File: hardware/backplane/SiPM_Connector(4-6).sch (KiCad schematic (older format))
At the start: 8 parts, among them J401 Conn_02x34_Odd_Even, J402 ERF8-060-05.0-L-DV, J403 Conn_02x34_Odd_Even, J501 Conn_02x34_Odd_Even-Connector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, J503 Conn_02x34_Odd_Even-Connector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, J601 Conn_02x34_Odd_Even-Connector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, J602 ERF8-060-05.0-L-DV, J603 Conn_02x34_Odd_Even-Connector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

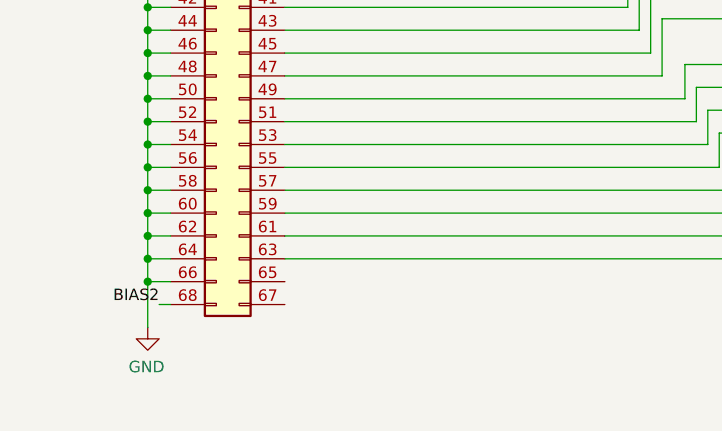
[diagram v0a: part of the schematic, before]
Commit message: Readout_FMC started
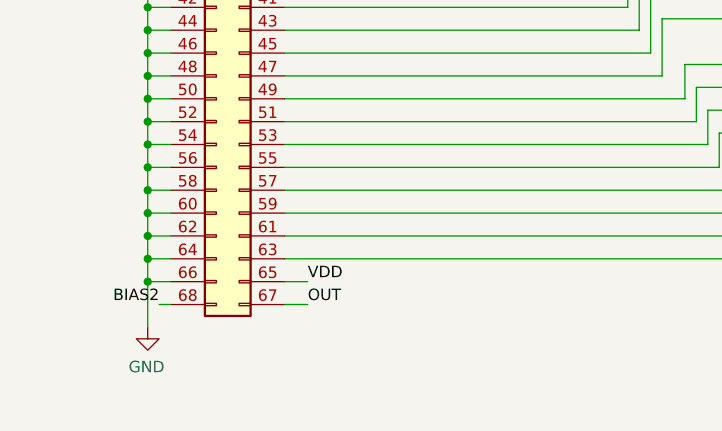
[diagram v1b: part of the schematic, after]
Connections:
- net OUT: now also J601.67 (Pin_67)
- net VDD: now also J601.65 (Pin_65)
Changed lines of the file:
@@
 	2050 4150 2050 4350
 $Comp
-L backplane-prototype-rescue:GND-power #PWR01
+L backplane-prototype-rescue:GND-power #PWR0107
 U 1 1 60B6FC2F
 P 2050 4350
-F 0 "#PWR01" H 2050 4100 50  0001 C CNN
+F 0 "#PWR0107" H 2050 4100 50  0001 C CNN
 F 1 "GND" H 2055 4177 50  0000 C CNN
 F 2 "" H 2050 4350 50  0001 C CNN
@@
 	8950 4150 8950 4350
 $Comp
-L backplane-prototype-rescue:GND-power #PWR06
+L backplane-prototype-rescue:GND-power #PWR0108
 U 1 1 60B6FC31
 P 8950 4350
-F 0 "#PWR06" H 8950 4100 50  0001 C CNN
+F 0 "#PWR0108" H 8950 4100 50  0001 C CNN
 F 1 "GND" H 8955 4177 50  0000 C CNN
 F 2 "" H 8950 4350 50  0001 C CNN
@@
 Connection ~ 6100 4600
 $Comp
-L backplane-prototype-rescue:GND-power #PWR0101
+L backplane-prototype-rescue:GND-power #PWR0109
 U 1 1 60B6FC33
 P 4900 13500
-F 0 "#PWR0101" H 4900 13250 50  0001 C CNN
+F 0 "#PWR0109" H 4900 13250 50  0001 C CNN
 F 1 "GND" H 4905 13327 50  0000 C CNN
 F 2 "" H 4900 13500 50  0001 C CNN
@@
 $EndComp
 $Comp
-L backplane-prototype-rescue:GND-power #PWR0102
+L backplane-prototype-rescue:GND-power #PWR0110
 U 1 1 63C65F05
 P 6100 13500
-F 0 "#PWR0102" H 6100 13250 50  0001 C CNN
+F 0 "#PWR0110" H 6100 13250 50  0001 C CNN
 F 1 "GND" H 6105 13327 50  0000 C CNN
 F 2 "" H 6100 13500 50  0001 C CNN
@@
 	2050 8700 2050 8900
 $Comp
-L backplane-prototype-rescue:GND-power #PWR?
+L backplane-prototype-rescue:GND-power #PWR0111
 U 1 1 63C65F08
 P 2050 8900
-F 0 "#PWR?" H 2050 8650 50  0001 C CNN
+F 0 "#PWR0111" H 2050 8650 50  0001 C CNN
 F 1 "GND" H 2055 8727 50  0000 C CNN
 F 2 "" H 2050 8900 50  0001 C CNN
@@
 	2050 13150 2050 13350
 $Comp
-L backplane-prototype-rescue:GND-power #PWR?
+L backplane-prototype-rescue:GND-power #PWR0112
 U 1 1 63C65F09
 P 2050 13350
-F 0 "#PWR?" H 2050 13100 50  0001 C CNN
+F 0 "#PWR0112" H 2050 13100 50  0001 C CNN
 F 1 "GND" H 2055 13177 50  0000 C CNN
 F 2 "" H 2050 13350 50  0001 C CNN
@@
 	8950 8700 8950 8900
 $Comp
-L backplane-prototype-rescue:GND-power #PWR?
+L backplane-prototype-rescue:GND-power #PWR0113
 U 1 1 63C65F0A
 P 8950 8900
-F 0 "#PWR?" H 8950 8650 50  0001 C CNN
+F 0 "#PWR0113" H 8950 8650 50  0001 C CNN
 F 1 "GND" H 8955 8727 50  0000 C CNN
 F 2 "" H 8950 8900 50  0001 C CNN
@@
 	8950 13150 8950 13350
 $Comp
-L backplane-prototype-rescue:GND-power #PWR?
+L backplane-prototype-rescue:GND-power #PWR0114
 U 1 1 63C65F0B
 P 8950 13350
-F 0 "#PWR?" H 8950 13100 50  0001 C CNN
+F 0 "#PWR0114" H 8950 13100 50  0001 C CNN
 F 1 "GND" H 8955 13177 50  0000 C CNN
 F 2 "" H 8950 13350 50  0001 C CNN
@@
 Wire Wire Line
 	8900 8800 8900 8900
+Text Label 2750 13150 0    50   ~ 0
+VDD
+Text Label 2750 13250 0    50   ~ 0
+OUT
+Wire Wire Line
+	2750 13250 2650 13250
+Wire Wire Line
+	2750 13150 2650 13150
 $EndSCHEMATC

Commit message: Backplane Layout Started
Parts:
- removed J401, J403: Conn_02x34_Odd_Even, Backplane-prototype:SAMTEC_CLM-134-02-F-D, symbol backplane-prototype-rescue:Conn_02x34_Odd_Even-Connector_Generic
- removed J402, J602: ERF8-060-05.0-L-DV, Backplane-prototype:ERF8-060-05.0-L-DV, symbol backplane-prototype-rescue:ERF8-060-XX.X-X-DV-ERF8-060-05.0-L-DV
- removed J501, J503, J601, J603: Conn_02x34_Odd_Even-Connector_Generic, symbol backplane-prototype-rescue:Conn_02x34_Odd_Even-Connector_Generic
- added J101, J103: Conn_02x34_Odd_Even, backplane:SAMTEC_CLM-134-02-F-D, symbol backplane-rescue:Conn_02x34_Odd_Even-Connector_Generic-backplane-prototype-resc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
- added J201, J203, J301, J303: Conn_02x34_Odd_Even-Connector_Generic, backplane:SAMTEC_CLM-134-02-F-D, symbol backplane-rescue:Conn_02x34_Odd_Even-Connector_Generic-backplane-prototype-resc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
- added J402, J602: ERF8-060-05.0-L-DV, backplane:ERF8-060-05.0-L-DV, symbol backplane-rescue:ERF8-060-XX.X-X-DV-ERF8-060-05.0-L-DV-backplane-prototype-resc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
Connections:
- net BCH0: now also J103.67 (Pin_67), J402.3
- net BCH1: now also J103.65 (Pin_65), J402.5
- net BCH10: now also J103.47 (Pin_47), J402.25
- net BCH11: now also J103.45 (Pin_45), J402.27
- net BCH12: now also J103.43 (Pin_43), J402.29
- net BCH13: now also J103.41 (Pin_41), J402.31
- net BCH14: now also J103.39 (Pin_39), J402.33
- net BCH15: now also J103.37 (Pin_37), J402.35
- net BCH16: now also J103.35 (Pin_35), J402.39
- net BCH17: now also J103.33 (Pin_33), J402.41
- net BCH18: now also J103.31 (Pin_31), J402.43
- net BCH19: now also J103.29 (Pin_29), J402.45
- net BCH2: now also J103.63 (Pin_63), J402.7
- net BCH20: now also J103.27 (Pin_27), J402.47
- net BCH21: now also J103.25 (Pin_25), J402.49
- net BCH22: now also J103.23 (Pin_23), J402.51
- net BCH23: now also J103.21 (Pin_21), J402.53
- net BCH24: now also J103.19 (Pin_19), J402.57
- net BCH25: now also J103.17 (Pin_17), J402.59
- net BCH26: now also J103.15 (Pin_15), J402.61
- net BCH27: now also J103.13 (Pin_13), J402.63
- net BCH28: now also J103.11 (Pin_11), J402.65
- net BCH29: now also J103.9 (Pin_9), J402.67
- net BCH3: now also J103.61 (Pin_61), J402.9
- net BCH30: now also J103.7 (Pin_7), J402.69
- net BCH31: now also J103.5 (Pin_5), J402.71
- net BCH4: now also J103.59 (Pin_59), J402.11
- net BCH5: now also J103.57 (Pin_57), J402.13
- net BCH6: now also J103.55 (Pin_55), J402.15
- net BCH7: now also J103.53 (Pin_53), J402.17
- net BCH8: now also J103.51 (Pin_51), J402.21
- net BCH9: now also J103.49 (Pin_49), J402.23
- net BIAS1: now also J101.2 (Pin_2), J201.2 (Pin_2), J301.2 (Pin_2), J402.76, J602.116, J602.36
- net BIAS2: now also J101.68 (Pin_68), J201.68 (Pin_68), J301.68 (Pin_68), J402.80, J602.120, J602.40
- net BIAS3: now also J103.68 (Pin_68), J203.68 (Pin_68), J303.68 (Pin_68), J402.75, J602.115, J602.35
- net BIAS4: now also J103.2 (Pin_2), J203.2 (Pin_2), J303.2 (Pin_2), J402.79, J602.119, J602.39
- net CH0: now also J101.1 (Pin_1), J402.4
- net CH1: now also J101.3 (Pin_3), J402.6
- net CH10: now also J101.21 (Pin_21), J402.26
- net CH11: now also J101.23 (Pin_23), J402.28
- net CH12: now also J101.25 (Pin_25), J402.30
- net CH13: now also J101.27 (Pin_27), J402.32
- net CH14: now also J101.29 (Pin_29), J402.34
- net CH15: now also J101.31 (Pin_31), J402.36
- net CH16: now also J101.33 (Pin_33), J402.40
- net CH17: now also J101.35 (Pin_35), J402.42
- net CH18: now also J101.37 (Pin_37), J402.44
- net CH19: now also J101.39 (Pin_39), J402.46
- net CH2: now also J101.5 (Pin_5), J402.8
- net CH20: now also J101.41 (Pin_41), J402.48
- net CH21: now also J101.43 (Pin_43), J402.50
- net CH22: now also J101.45 (Pin_45), J402.52
- net CH23: now also J101.47 (Pin_47), J402.54
- net CH24: now also J101.49 (Pin_49), J402.58
- net CH25: now also J101.51 (Pin_51), J402.60
- net CH26: now also J101.53 (Pin_53), J402.62
- net CH27: now also J101.55 (Pin_55), J402.64
- net CH28: now also J101.57 (Pin_57), J402.66
- net CH29: now also J101.59 (Pin_59), J402.68
- net CH3: now also J101.7 (Pin_7), J402.10
- net CH30: now also J101.61 (Pin_61), J402.70
- net CH31: now also J101.63 (Pin_63), J402.72
- net CH4: now also J101.9 (Pin_9), J402.12
- net CH5: now also J101.11 (Pin_11), J402.14
- net CH6: now also J101.13 (Pin_13), J402.16
- net CH7: now also J101.15 (Pin_15), J402.18
- net CH8: now also J101.17 (Pin_17), J402.22
- net CH9: now also J101.19 (Pin_19), J402.24
- net GND: now also J101.10 (Pin_10), J101.12 (Pin_12), J101.14 (Pin_14), J101.16 (Pin_16), J101.18 (Pin_18), J101.20 (Pin_20), J101.22 (Pin_22), J101.24 (Pin_24), J101.26 (Pin_26), J101.28 (Pin_28), J101.30 (Pin_30), J101.32 (Pin_32), J101.34 (Pin_34), J101.36 (Pin_36), J101.38 (Pin_38), J101.4 (Pin_4), J101.40 (Pin_40), J101.42 (Pin_42), J101.44 (Pin_44), J101.46 (Pin_46), J101.48 (Pin_48), J101.50 (Pin_50), J101.52 (Pin_52), J101.54 (Pin_54), J101.56 (Pin_56), J101.58 (Pin_58), J101.6 (Pin_6), J101.60 (Pin_60), J101.62 (Pin_62), J101.64 (Pin_64), J101.66 (Pin_66), J101.8 (Pin_8), J103.10 (Pin_10), J103.12 (Pin_12), J103.14 (Pin_14), J103.16 (Pin_16), J103.18 (Pin_18), J103.20 (Pin_20), J103.22 (Pin_22), J103.24 (Pin_24), J103.26 (Pin_26), J103.28 (Pin_28), J103.30 (Pin_30), J103.32 (Pin_32), J103.34 (Pin_34), J103.36 (Pin_36), J103.38 (Pin_38), J103.4 (Pin_4), J103.40 (Pin_40), J103.42 (Pin_42), J103.44 (Pin_44), J103.46 (Pin_46), J103.48 (Pin_48), J103.50 (Pin_50), J103.52 (Pin_52), J103.54 (Pin_54), J103.56 (Pin_56), J103.58 (Pin_58), J103.6 (Pin_6), J103.60 (Pin_60), J103.62 (Pin_62), J103.64 (Pin_64), J103.66 (Pin_66), J103.8 (Pin_8), J201.10 (Pin_10), J201.12 (Pin_12), J201.14 (Pin_14), J201.16 (Pin_16), J201.18 (Pin_18), J201.20 (Pin_20), J201.22 (Pin_22), J201.24 (Pin_24), J201.26 (Pin_26), J201.28 (Pin_28), J201.30 (Pin_30), J201.32 (Pin_32), J201.34 (Pin_34), J201.36 (Pin_36), J201.38 (Pin_38), J201.4 (Pin_4), J201.40 (Pin_40), J201.42 (Pin_42), J201.44 (Pin_44), J201.46 (Pin_46), J201.48 (Pin_48), J201.50 (Pin_50), J201.52 (Pin_52), J201.54 (Pin_54), J201.56 (Pin_56), J201.58 (Pin_58), J201.6 (Pin_6), J201.60 (Pin_60), J201.62 (Pin_62), J201.64 (Pin_64), J201.66 (Pin_66), J201.8 (Pin_8), J203.10 (Pin_10), J203.12 (Pin_12), J203.14 (Pin_14), J203.16 (Pin_16), J203.18 (Pin_18), J203.20 (Pin_20), J203.22 (Pin_22), J203.24 (Pin_24), J203.26 (Pin_26), J203.28 (Pin_28), J203.30 (Pin_30), J203.32 (Pin_32), J203.34 (Pin_34), J203.36 (Pin_36), J203.38 (Pin_38), J203.4 (Pin_4), J203.40 (Pin_40), J203.42 (Pin_42), J203.44 (Pin_44), J203.46 (Pin_46), J203.48 (Pin_48), J203.50 (Pin_50), J203.52 (Pin_52), J203.54 (Pin_54), J203.56 (Pin_56), J203.58 (Pin_58), J203.6 (Pin_6), J203.60 (Pin_60), J203.62 (Pin_62), J203.64 (Pin_64), J203.66 (Pin_66), J203.8 (Pin_8), J301.10 (Pin_10), J301.12 (Pin_12), J301.14 (Pin_14), J301.16 (Pin_16), J301.18 (Pin_18), J301.20 (Pin_20), J301.22 (Pin_22), J301.24 (Pin_24), J301.26 (Pin_26), J301.28 (Pin_28), J301.30 (Pin_30), J301.32 (Pin_32), J301.34 (Pin_34), J301.36 (Pin_36), J301.38 (Pin_38), J301.4 (Pin_4), J301.40 (Pin_40), J301.42 (Pin_42), J301.44 (Pin_44), J301.46 (Pin_46), J301.48 (Pin_48), J301.50 (Pin_50), J301.52 (Pin_52), J301.54 (Pin_54), J301.56 (Pin_56), J301.58 (Pin_58), J301.6 (Pin_6), J301.60 (Pin_60), J301.62 (Pin_62), J301.64 (Pin_64), J301.66 (Pin_66), J301.8 (Pin_8), J303.10 (Pin_10), J303.12 (Pin_12), J303.14 (Pin_14), J303.16 (Pin_16), J303.18 (Pin_18), J303.20 (Pin_20), J303.22 (Pin_22), J303.24 (Pin_24), J303.26 (Pin_26), J303.28 (Pin_28), J303.30 (Pin_30), J303.32 (Pin_32), J303.34 (Pin_34), J303.36 (Pin_36), J303.38 (Pin_38), J303.4 (Pin_4), J303.40 (Pin_40), J303.42 (Pin_42), J303.44 (Pin_44), J303.46 (Pin_46), J303.48 (Pin_48), J303.50 (Pin_50), J303.52 (Pin_52), J303.54 (Pin_54), J303.56 (Pin_56), J303.58 (Pin_58), J303.6 (Pin_6), J303.60 (Pin_60), J303.62 (Pin_62), J303.64 (Pin_64), J303.66 (Pin_66), J303.8 (Pin_8), J402.1, J402.100, J402.117, J402.118, J402.19, J402.2, J402.20, J402.37, J402.38, J402.55, J402.56, J402.73, J402.74, J402.81, J402.82, J402.99, J602.113, J602.114, J602.15, J602.16, J602.33, J602.34, J602.41, J602.42, J602.59, J602.60, J602.77, J602.78, J602.95, J602.96
- net OUT: now also J101.67 (Pin_67), J201.67 (Pin_67), J301.67 (Pin_67), J402.77, J602.117, J602.37
- net VDD: now also J101.65 (Pin_65), J201.65 (Pin_65), J301.65 (Pin_65), J402.78, J602.118, J602.38
- new net BCH32: J203.67 (Pin_67), J402.83
- new net BCH33: J203.65 (Pin_65), J402.85
- new net BCH34: J203.63 (Pin_63), J402.87
- new net BCH35: J203.61 (Pin_61), J402.89
- new net BCH36: J203.59 (Pin_59), J402.91
- new net BCH37: J203.57 (Pin_57), J402.93
- new net BCH38: J203.55 (Pin_55), J402.95
- new net BCH39: J203.53 (Pin_53), J402.97
- new net BCH40: J203.51 (Pin_51), J402.101
- new net BCH41: J203.49 (Pin_49), J402.103
- new net BCH42: J203.47 (Pin_47), J402.105
- new net BCH43: J203.45 (Pin_45), J402.107
- new net BCH44: J203.43 (Pin_43), J402.109
- new net BCH45: J203.41 (Pin_41), J402.111
- new net BCH46: J203.39 (Pin_39), J402.113
- new net BCH47: J203.37 (Pin_37), J402.115
- new net BCH48: J203.35 (Pin_35), J402.119
- new net BCH49: J203.33 (Pin_33), J602.1
- new net BCH50: J203.31 (Pin_31), J602.3
- new net BCH51: J203.29 (Pin_29), J602.5
- new net BCH52: J203.27 (Pin_27), J602.7
- new net BCH53: J203.25 (Pin_25), J602.9
- new net BCH54: J203.23 (Pin_23), J602.11
- new net BCH55: J203.21 (Pin_21), J602.13
- new net BCH56: J203.19 (Pin_19), J602.17
- new net BCH57: J203.17 (Pin_17), J602.19
- new net BCH58: J203.15 (Pin_15), J602.21
- new net BCH59: J203.13 (Pin_13), J602.23
- new net BCH60: J203.11 (Pin_11), J602.25
- new net BCH61: J203.9 (Pin_9), J602.27
- new net BCH62: J203.7 (Pin_7), J602.29
- new net BCH63: J203.5 (Pin_5), J602.31
- new net BCH64: J303.67 (Pin_67), J602.43
- new net BCH65: J303.65 (Pin_65), J602.45
- new net BCH66: J303.63 (Pin_63), J602.47
- new net BCH67: J303.61 (Pin_61), J602.49
- new net BCH68: J303.59 (Pin_59), J602.51
- new net BCH69: J303.57 (Pin_57), J602.53
- new net BCH70: J303.55 (Pin_55), J602.55
- new net BCH71: J303.53 (Pin_53), J602.57
- new net BCH72: J303.51 (Pin_51), J602.61
- new net BCH73: J303.49 (Pin_49), J602.63
- new net BCH74: J303.47 (Pin_47), J602.65
- new net BCH75: J303.45 (Pin_45), J602.67
- new net BCH76: J303.43 (Pin_43), J602.69
- new net BCH77: J303.41 (Pin_41), J602.71
- new net BCH78: J303.39 (Pin_39), J602.73
- new net BCH79: J303.37 (Pin_37), J602.75
- new net BCH80: J303.35 (Pin_35), J602.79
- new net BCH81: J303.33 (Pin_33), J602.81
- new net BCH82: J303.31 (Pin_31), J602.83
- new net BCH83: J303.29 (Pin_29), J602.85
- new net BCH84: J303.27 (Pin_27), J602.87
- new net BCH85: J303.25 (Pin_25), J602.89
- new net BCH86: J303.23 (Pin_23), J602.91
- new net BCH87: J303.21 (Pin_21), J602.93
- new net BCH88: J303.19 (Pin_19), J602.97
- new net BCH89: J303.17 (Pin_17), J602.99
- new net BCH90: J303.15 (Pin_15), J602.101
- new net BCH91: J303.13 (Pin_13), J602.103
- new net BCH92: J303.11 (Pin_11), J602.105
- new net BCH93: J303.9 (Pin_9), J602.107
- new net BCH94: J303.7 (Pin_7), J602.109
- new net BCH95: J303.5 (Pin_5), J602.111
- new net CH32: J201.1 (Pin_1), J402.84
- new net CH33: J201.3 (Pin_3), J402.86
- new net CH34: J201.5 (Pin_5), J402.88
- new net CH35: J201.7 (Pin_7), J402.90
- new net CH36: J201.9 (Pin_9), J402.92
- new net CH37: J201.11 (Pin_11), J402.94
- new net CH38: J201.13 (Pin_13), J402.96
- new net CH39: J201.15 (Pin_15), J402.98
- new net CH40: J201.17 (Pin_17), J402.102
- new net CH41: J201.19 (Pin_19), J402.104
- new net CH42: J201.21 (Pin_21), J402.106
- new net CH43: J201.23 (Pin_23), J402.108
- new net CH44: J201.25 (Pin_25), J402.110
- new net CH45: J201.27 (Pin_27), J402.112
- new net CH46: J201.29 (Pin_29), J402.114
- new net CH47: J201.31 (Pin_31), J402.116
- new net CH48: J201.33 (Pin_33), J402.120
- new net CH49: J201.35 (Pin_35), J602.2
- new net CH50: J201.37 (Pin_37), J602.4
- new net CH51: J201.39 (Pin_39), J602.6
- new net CH52: J201.41 (Pin_41), J602.8
- new net CH53: J201.43 (Pin_43), J602.10
- new net CH54: J201.45 (Pin_45), J602.12
- new net CH55: J201.47 (Pin_47), J602.14
- new net CH56: J201.49 (Pin_49), J602.18
- new net CH57: J201.51 (Pin_51), J602.20
- new net CH58: J201.53 (Pin_53), J602.22
- new net CH59: J201.55 (Pin_55), J602.24
- new net CH60: J201.57 (Pin_57), J602.26
- new net CH61: J201.59 (Pin_59), J602.28
- new net CH62: J201.61 (Pin_61), J602.30
- new net CH63: J201.63 (Pin_63), J602.32
- new net CH64: J301.1 (Pin_1), J602.44
- new net CH65: J301.3 (Pin_3), J602.46
- new net CH66: J301.5 (Pin_5), J602.48
- new net CH67: J301.7 (Pin_7), J602.50
- new net CH68: J301.9 (Pin_9), J602.52
- new net CH69: J301.11 (Pin_11), J602.54
- new net CH70: J301.13 (Pin_13), J602.56
- new net CH71: J301.15 (Pin_15), J602.58
- new net CH72: J301.17 (Pin_17), J602.62
- new net CH73: J301.19 (Pin_19), J602.64
- new net CH74: J301.21 (Pin_21), J602.66
- new net CH75: J301.23 (Pin_23), J602.68
- new net CH76: J301.25 (Pin_25), J602.70
- new net CH77: J301.27 (Pin_27), J602.72
- new net CH78: J301.29 (Pin_29), J602.74
- new net CH79: J301.31 (Pin_31), J602.76
- new net CH80: J301.33 (Pin_33), J602.80
- new net CH81: J301.35 (Pin_35), J602.82
- new net CH82: J301.37 (Pin_37), J602.84
- new net CH83: J301.39 (Pin_39), J602.86
- new net CH84: J301.41 (Pin_41), J602.88
- new net CH85: J301.43 (Pin_43), J602.90
- new net CH86: J301.45 (Pin_45), J602.92
- new net CH87: J301.47 (Pin_47), J602.94
- new net CH88: J301.49 (Pin_49), J602.98
- new net CH89: J301.51 (Pin_51), J602.100
- new net CH90: J301.53 (Pin_53), J602.102
- new net CH91: J301.55 (Pin_55), J602.104
- new net CH92: J301.57 (Pin_57), J602.106
- new net CH93: J301.59 (Pin_59), J602.108
- new net CH94: J301.61 (Pin_61), J602.110
- new net CH95: J301.63 (Pin_63), J602.112
- no-connect marks 3 -> 6

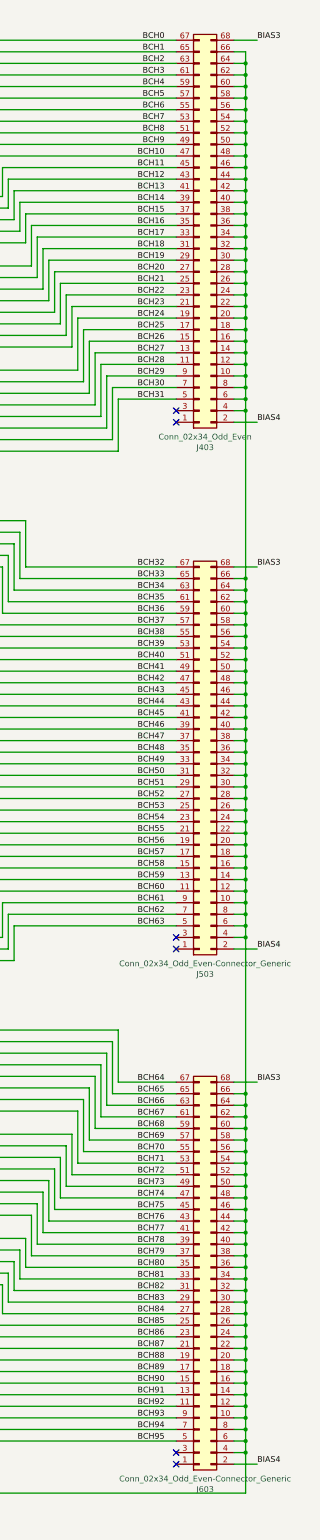
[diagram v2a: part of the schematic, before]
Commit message: SiPM Board RevC layout modified
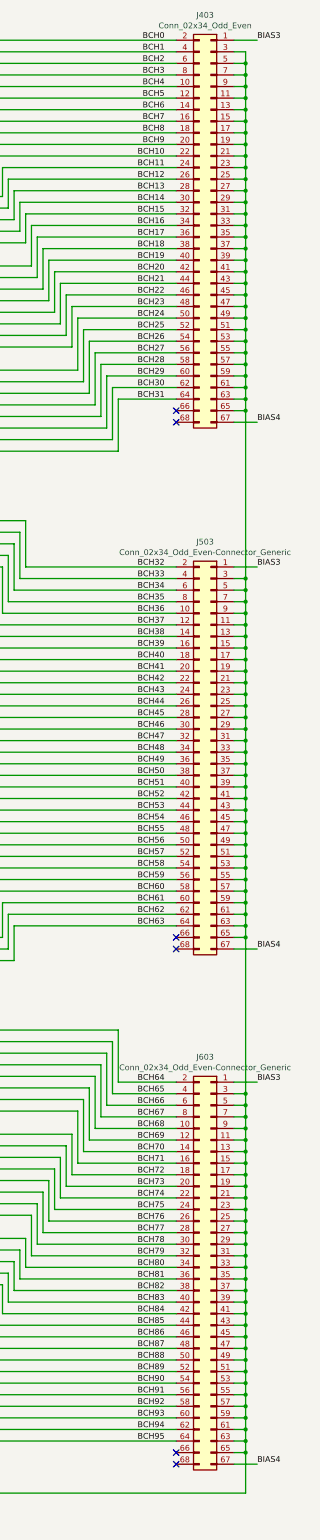
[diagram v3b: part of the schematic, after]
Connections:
- net BCH0: now also J103.2 (Pin_2); no longer J103.67 (Pin_67)
- net BCH1: now also J103.4 (Pin_4); no longer J103.65 (Pin_65)
- net BCH10: now also J103.22 (Pin_22); no longer J103.47 (Pin_47)
- net BCH11: now also J103.24 (Pin_24); no longer J103.45 (Pin_45)
- net BCH12: now also J103.26 (Pin_26); no longer J103.43 (Pin_43)
- net BCH13: now also J103.28 (Pin_28); no longer J103.41 (Pin_41)
- net BCH14: now also J103.30 (Pin_30); no longer J103.39 (Pin_39)
- net BCH15: now also J103.32 (Pin_32); no longer J103.37 (Pin_37)
- net BCH16: now also J103.34 (Pin_34); no longer J103.35 (Pin_35)
- net BCH17: now also J103.36 (Pin_36); no longer J103.33 (Pin_33)
- net BCH18: now also J103.38 (Pin_38); no longer J103.31 (Pin_31)
- net BCH19: now also J103.40 (Pin_40); no longer J103.29 (Pin_29)
- net BCH2: now also J103.6 (Pin_6); no longer J103.63 (Pin_63)
- net BCH20: now also J103.42 (Pin_42); no longer J103.27 (Pin_27)
- net BCH21: now also J103.44 (Pin_44); no longer J103.25 (Pin_25)
- net BCH22: now also J103.46 (Pin_46); no longer J103.23 (Pin_23)
- net BCH23: now also J103.48 (Pin_48); no longer J103.21 (Pin_21)
- net BCH24: now also J103.50 (Pin_50); no longer J103.19 (Pin_19)
- net BCH25: now also J103.52 (Pin_52); no longer J103.17 (Pin_17)
- net BCH26: now also J103.54 (Pin_54); no longer J103.15 (Pin_15)
- net BCH27: now also J103.56 (Pin_56); no longer J103.13 (Pin_13)
- net BCH28: now also J103.58 (Pin_58); no longer J103.11 (Pin_11)
- net BCH29: now also J103.60 (Pin_60); no longer J103.9 (Pin_9)
- net BCH3: now also J103.8 (Pin_8); no longer J103.61 (Pin_61)
- net BCH30: now also J103.62 (Pin_62); no longer J103.7 (Pin_7)
- net BCH31: now also J103.64 (Pin_64); no longer J103.5 (Pin_5)
- net BCH32: now also J203.2 (Pin_2); no longer J203.67 (Pin_67)
- net BCH33: now also J203.4 (Pin_4); no longer J203.65 (Pin_65)
- net BCH34: now also J203.6 (Pin_6); no longer J203.63 (Pin_63)
- net BCH35: now also J203.8 (Pin_8); no longer J203.61 (Pin_61)
- net BCH36: now also J203.10 (Pin_10); no longer J203.59 (Pin_59)
- net BCH37: now also J203.12 (Pin_12); no longer J203.57 (Pin_57)
- net BCH38: now also J203.14 (Pin_14); no longer J203.55 (Pin_55)
- net BCH39: now also J203.16 (Pin_16); no longer J203.53 (Pin_53)
- net BCH4: now also J103.10 (Pin_10); no longer J103.59 (Pin_59)
- net BCH40: now also J203.18 (Pin_18); no longer J203.51 (Pin_51)
- net BCH41: now also J203.20 (Pin_20); no longer J203.49 (Pin_49)
- net BCH42: now also J203.22 (Pin_22); no longer J203.47 (Pin_47)
- net BCH43: now also J203.24 (Pin_24); no longer J203.45 (Pin_45)
- net BCH44: now also J203.26 (Pin_26); no longer J203.43 (Pin_43)
- net BCH45: now also J203.28 (Pin_28); no longer J203.41 (Pin_41)
- net BCH46: now also J203.30 (Pin_30); no longer J203.39 (Pin_39)
- net BCH47: now also J203.32 (Pin_32); no longer J203.37 (Pin_37)
- net BCH48: now also J203.34 (Pin_34); no longer J203.35 (Pin_35)
- net BCH49: now also J203.36 (Pin_36); no longer J203.33 (Pin_33)
- net BCH5: now also J103.12 (Pin_12); no longer J103.57 (Pin_57)
- net BCH50: now also J203.38 (Pin_38); no longer J203.31 (Pin_31)
- net BCH51: now also J203.40 (Pin_40); no longer J203.29 (Pin_29)
- net BCH52: now also J203.42 (Pin_42); no longer J203.27 (Pin_27)
- net BCH53: now also J203.44 (Pin_44); no longer J203.25 (Pin_25)
- net BCH54: now also J203.46 (Pin_46); no longer J203.23 (Pin_23)
- net BCH55: now also J203.48 (Pin_48); no longer J203.21 (Pin_21)
- net BCH56: now also J203.50 (Pin_50); no longer J203.19 (Pin_19)
- net BCH57: now also J203.52 (Pin_52); no longer J203.17 (Pin_17)
- net BCH58: now also J203.54 (Pin_54); no longer J203.15 (Pin_15)
- net BCH59: now also J203.56 (Pin_56); no longer J203.13 (Pin_13)
- net BCH6: now also J103.14 (Pin_14); no longer J103.55 (Pin_55)
- net BCH60: now also J203.58 (Pin_58); no longer J203.11 (Pin_11)
- net BCH61: now also J203.60 (Pin_60); no longer J203.9 (Pin_9)
- net BCH62: now also J203.62 (Pin_62); no longer J203.7 (Pin_7)
- net BCH63: now also J203.64 (Pin_64); no longer J203.5 (Pin_5)
- net BCH64: now also J303.2 (Pin_2); no longer J303.67 (Pin_67)
- net BCH65: now also J303.4 (Pin_4); no longer J303.65 (Pin_65)
- net BCH66: now also J303.6 (Pin_6); no longer J303.63 (Pin_63)
- net BCH67: now also J303.8 (Pin_8); no longer J303.61 (Pin_61)
- net BCH68: now also J303.10 (Pin_10); no longer J303.59 (Pin_59)
- net BCH69: now also J303.12 (Pin_12); no longer J303.57 (Pin_57)
- net BCH7: now also J103.16 (Pin_16); no longer J103.53 (Pin_53)
- net BCH70: now also J303.14 (Pin_14); no longer J303.55 (Pin_55)
- net BCH71: now also J303.16 (Pin_16); no longer J303.53 (Pin_53)
- net BCH72: now also J303.18 (Pin_18); no longer J303.51 (Pin_51)
- net BCH73: now also J303.20 (Pin_20); no longer J303.49 (Pin_49)
- net BCH74: now also J303.22 (Pin_22); no longer J303.47 (Pin_47)
- net BCH75: now also J303.24 (Pin_24); no longer J303.45 (Pin_45)
- net BCH76: now also J303.26 (Pin_26); no longer J303.43 (Pin_43)
- net BCH77: now also J303.28 (Pin_28); no longer J303.41 (Pin_41)
- net BCH78: now also J303.30 (Pin_30); no longer J303.39 (Pin_39)
- net BCH79: now also J303.32 (Pin_32); no longer J303.37 (Pin_37)
- net BCH8: now also J103.18 (Pin_18); no longer J103.51 (Pin_51)
- net BCH80: now also J303.34 (Pin_34); no longer J303.35 (Pin_35)
- net BCH81: now also J303.36 (Pin_36); no longer J303.33 (Pin_33)
- net BCH82: now also J303.38 (Pin_38); no longer J303.31 (Pin_31)
- net BCH83: now also J303.40 (Pin_40); no longer J303.29 (Pin_29)
- net BCH84: now also J303.42 (Pin_42); no longer J303.27 (Pin_27)
- net BCH85: now also J303.44 (Pin_44); no longer J303.25 (Pin_25)
- net BCH86: now also J303.46 (Pin_46); no longer J303.23 (Pin_23)
- net BCH87: now also J303.48 (Pin_48); no longer J303.21 (Pin_21)
- net BCH88: now also J303.50 (Pin_50); no longer J303.19 (Pin_19)
- net BCH89: now also J303.52 (Pin_52); no longer J303.17 (Pin_17)
- net BCH9: now also J103.20 (Pin_20); no longer J103.49 (Pin_49)
- net BCH90: now also J303.54 (Pin_54); no longer J303.15 (Pin_15)
- net BCH91: now also J303.56 (Pin_56); no longer J303.13 (Pin_13)
- net BCH92: now also J303.58 (Pin_58); no longer J303.11 (Pin_11)
- net BCH93: now also J303.60 (Pin_60); no longer J303.9 (Pin_9)
- net BCH94: now also J303.62 (Pin_62); no longer J303.7 (Pin_7)
- net BCH95: now also J303.64 (Pin_64); no longer J303.5 (Pin_5)
- net BIAS3: now also J103.1 (Pin_1), J203.1 (Pin_1), J303.1 (Pin_1); no longer J103.68 (Pin_68), J203.68 (Pin_68), J303.68 (Pin_68)
- net BIAS4: now also J103.67 (Pin_67), J203.67 (Pin_67), J303.67 (Pin_67); no longer J103.2 (Pin_2), J203.2 (Pin_2), J303.2 (Pin_2)
- net GND: now also J103.11 (Pin_11), J103.13 (Pin_13), J103.15 (Pin_15), J103.17 (Pin_17), J103.19 (Pin_19), J103.21 (Pin_21), J103.23 (Pin_23), J103.25 (Pin_25), J103.27 (Pin_27), J103.29 (Pin_29), J103.3 (Pin_3), J103.31 (Pin_31), J103.33 (Pin_33), J103.35 (Pin_35), J103.37 (Pin_37), J103.39 (Pin_39), J103.41 (Pin_41), J103.43 (Pin_43), J103.45 (Pin_45), J103.47 (Pin_47), J103.49 (Pin_49), J103.5 (Pin_5), J103.51 (Pin_51), J103.53 (Pin_53), J103.55 (Pin_55), J103.57 (Pin_57), J103.59 (Pin_59), J103.61 (Pin_61), J103.63 (Pin_63), J103.65 (Pin_65), J103.7 (Pin_7), J103.9 (Pin_9), J203.11 (Pin_11), J203.13 (Pin_13), J203.15 (Pin_15), J203.17 (Pin_17), J203.19 (Pin_19), J203.21 (Pin_21), J203.23 (Pin_23), J203.25 (Pin_25), J203.27 (Pin_27), J203.29 (Pin_29), J203.3 (Pin_3), J203.31 (Pin_31), J203.33 (Pin_33), J203.35 (Pin_35), J203.37 (Pin_37), J203.39 (Pin_39), J203.41 (Pin_41), J203.43 (Pin_43), J203.45 (Pin_45), J203.47 (Pin_47), J203.49 (Pin_49), J203.5 (Pin_5), J203.51 (Pin_51), J203.53 (Pin_53), J203.55 (Pin_55), J203.57 (Pin_57), J203.59 (Pin_59), J203.61 (Pin_61), J203.63 (Pin_63), J203.65 (Pin_65), J203.7 (Pin_7), J203.9 (Pin_9), J303.11 (Pin_11), J303.13 (Pin_13), J303.15 (Pin_15), J303.17 (Pin_17), J303.19 (Pin_19), J303.21 (Pin_21), J303.23 (Pin_23), J303.25 (Pin_25), J303.27 (Pin_27), J303.29 (Pin_29), J303.3 (Pin_3), J303.31 (Pin_31), J303.33 (Pin_33), J303.35 (Pin_35), J303.37 (Pin_37), J303.39 (Pin_39), J303.41 (Pin_41), J303.43 (Pin_43), J303.45 (Pin_45), J303.47 (Pin_47), J303.49 (Pin_49), J303.5 (Pin_5), J303.51 (Pin_51), J303.53 (Pin_53), J303.55 (Pin_55), J303.57 (Pin_57), J303.59 (Pin_59), J303.61 (Pin_61), J303.63 (Pin_63), J303.65 (Pin_65), J303.7 (Pin_7), J303.9 (Pin_9); no longer J103.10 (Pin_10), J103.12 (Pin_12), J103.14 (Pin_14), J103.16 (Pin_16), J103.18 (Pin_18), J103.20 (Pin_20), J103.22 (Pin_22), J103.24 (Pin_24), J103.26 (Pin_26), J103.28 (Pin_28), J103.30 (Pin_30), J103.32 (Pin_32), J103.34 (Pin_34), J103.36 (Pin_36), J103.38 (Pin_38), J103.4 (Pin_4), J103.40 (Pin_40), J103.42 (Pin_42), J103.44 (Pin_44), J103.46 (Pin_46), J103.48 (Pin_48), J103.50 (Pin_50), J103.52 (Pin_52), J103.54 (Pin_54), J103.56 (Pin_56), J103.58 (Pin_58), J103.6 (Pin_6), J103.60 (Pin_60), J103.62 (Pin_62), J103.64 (Pin_64), J103.66 (Pin_66), J103.8 (Pin_8), J203.10 (Pin_10), J203.12 (Pin_12), J203.14 (Pin_14), J203.16 (Pin_16), J203.18 (Pin_18), J203.20 (Pin_20), J203.22 (Pin_22), J203.24 (Pin_24), J203.26 (Pin_26), J203.28 (Pin_28), J203.30 (Pin_30), J203.32 (Pin_32), J203.34 (Pin_34), J203.36 (Pin_36), J203.38 (Pin_38), J203.4 (Pin_4), J203.40 (Pin_40), J203.42 (Pin_42), J203.44 (Pin_44), J203.46 (Pin_46), J203.48 (Pin_48), J203.50 (Pin_50), J203.52 (Pin_52), J203.54 (Pin_54), J203.56 (Pin_56), J203.58 (Pin_58), J203.6 (Pin_6), J203.60 (Pin_60), J203.62 (Pin_62), J203.64 (Pin_64), J203.66 (Pin_66), J203.8 (Pin_8), J303.10 (Pin_10), J303.12 (Pin_12), J303.14 (Pin_14), J303.16 (Pin_16), J303.18 (Pin_18), J303.20 (Pin_20), J303.22 (Pin_22), J303.24 (Pin_24), J303.26 (Pin_26), J303.28 (Pin_28), J303.30 (Pin_30), J303.32 (Pin_32), J303.34 (Pin_34), J303.36 (Pin_36), J303.38 (Pin_38), J303.4 (Pin_4), J303.40 (Pin_40), J303.42 (Pin_42), J303.44 (Pin_44), J303.46 (Pin_46), J303.48 (Pin_48), J303.50 (Pin_50), J303.52 (Pin_52), J303.54 (Pin_54), J303.56 (Pin_56), J303.58 (Pin_58), J303.6 (Pin_6), J303.60 (Pin_60), J303.62 (Pin_62), J303.64 (Pin_64), J303.66 (Pin_66), J303.8 (Pin_8)
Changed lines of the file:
@@
 L backplane-rescue:Conn_02x34_Odd_Even-Connector_Generic-backplane-prototype-rescue J103
 U 1 1 682C5400
-P 8550 4000
+P 8650 3900
 AR Path="/682C5400" Ref="J103"  Part="1"
 AR Path="/60955FE3/682C5400" Ref="J103"  Part="1"
 AR Path="/60A16277/682C5400" Ref="J403"  Part="1"
-F 0 "J403" H 8600 5817 50  0000 C CNN
-F 1 "Conn_02x34_Odd_Even" H 8600 5726 50  0000 C CNN
-F 2 "backplane:SAMTEC_CLM-134-02-F-D" H 8550 4000 50  0001 C CNN
-F 3 "http://suddendocs.samtec.com/catalog_english/clm_sm.pdf" H 8550 4000 50  0001 C CNN
-F 4 "CLM-134-02-F-D" H 8550 4000 50  0001 C CNN "MFN"
-F 5 "Digi-Key" H 8550 4000 50  0001 C CNN "Supplier"
-F 6 "CLM-134-02-F-D-ND" H 8550 4000 50  0001 C CNN "Supplier P/N"
-F 7 "$9.02" H 8550 4000 50  0001 C CNN "Item Cost"
-	1    8550 4000
-	1    0    0    1
+F 0 "J403" H 8700 5717 50  0000 C CNN
+F 1 "Conn_02x34_Odd_Even" H 8700 5626 50  0000 C CNN
+F 2 "backplane:SAMTEC_CLM-134-02-F-D" H 8650 3900 50  0001 C CNN
+F 3 "http://suddendocs.samtec.com/catalog_english/clm_sm.pdf" H 8650 3900 50  0001 C CNN
+F 4 "CLM-134-02-F-D" H 8650 3900 50  0001 C CNN "MFN"
+F 5 "Digi-Key" H 8650 3900 50  0001 C CNN "Supplier"
+F 6 "CLM-134-02-F-D-ND" H 8650 3900 50  0001 C CNN "Supplier P/N"
+F 7 "$9.02" H 8650 3900 50  0001 C CNN "Item Cost"
+	1    8650 3900
+	-1   0    0    -1
 $EndComp
 $Comp
@@
 L backplane-rescue:Conn_02x34_Odd_Even-Connector_Generic-backplane-prototype-rescue J303
 U 1 1 682C53FD
-P 8550 13000
+P 8650 12900
 AR Path="/682C53FD" Ref="J303"  Part="1"
 AR Path="/60955FE3/682C53FD" Ref="J303"  Part="1"
 AR Path="/60A16277/682C53FD" Ref="J603"  Part="1"
-F 0 "J603" H 8600 14817 50  0000 C CNN
-F 1 "Conn_02x34_Odd_Even-Connector_Generic" H 8600 14726 50  0000 C CNN
-F 2 "backplane:SAMTEC_CLM-134-02-F-D" H 8550 13000 50  0001 C CNN
-F 3 "" H 8550 13000 50  0001 C CNN
-	1    8550 13000
-	1    0    0    1
+F 0 "J603" H 8700 14717 50  0000 C CNN
+F 1 "Conn_02x34_Odd_Even-Connector_Generic" H 8700 14626 50  0000 C CNN
+F 2 "backplane:SAMTEC_CLM-134-02-F-D" H 8650 12900 50  0001 C CNN
+F 3 "" H 8650 12900 50  0001 C CNN
+	1    8650 12900
+	-1   0    0    -1
 $EndComp
 $Comp
@@
 L backplane-rescue:Conn_02x34_Odd_Even-Connector_Generic-backplane-prototype-rescue J203
 U 1 1 682C53FC
-P 8550 8550
+P 8650 8450
 AR Path="/682C53FC" Ref="J203"  Part="1"
 AR Path="/60955FE3/682C53FC" Ref="J203"  Part="1"
 AR Path="/60A16277/682C53FC" Ref="J503"  Part="1"
-F 0 "J503" H 8600 10367 50  0000 C CNN
-F 1 "Conn_02x34_Odd_Even-Connector_Generic" H 8600 10276 50  0000 C CNN
-F 2 "backplane:SAMTEC_CLM-134-02-F-D" H 8550 8550 50  0001 C CNN
-F 3 "" H 8550 8550 50  0001 C CNN
-	1    8550 8550
-	1    0    0    1
+F 0 "J503" H 8700 10267 50  0000 C CNN
+F 1 "Conn_02x34_Odd_Even-Connector_Generic" H 8700 10176 50  0000 C CNN
+F 2 "backplane:SAMTEC_CLM-134-02-F-D" H 8650 8450 50  0001 C CNN
+F 3 "" H 8650 8450 50  0001 C CNN
+	1    8650 8450
+	-1   0    0    -1
 $EndComp
 NoConn ~ 8350 10150
